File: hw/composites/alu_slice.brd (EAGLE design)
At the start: 50 x 50 mm, 10 parts, among them CON2 GENERIC-2X10

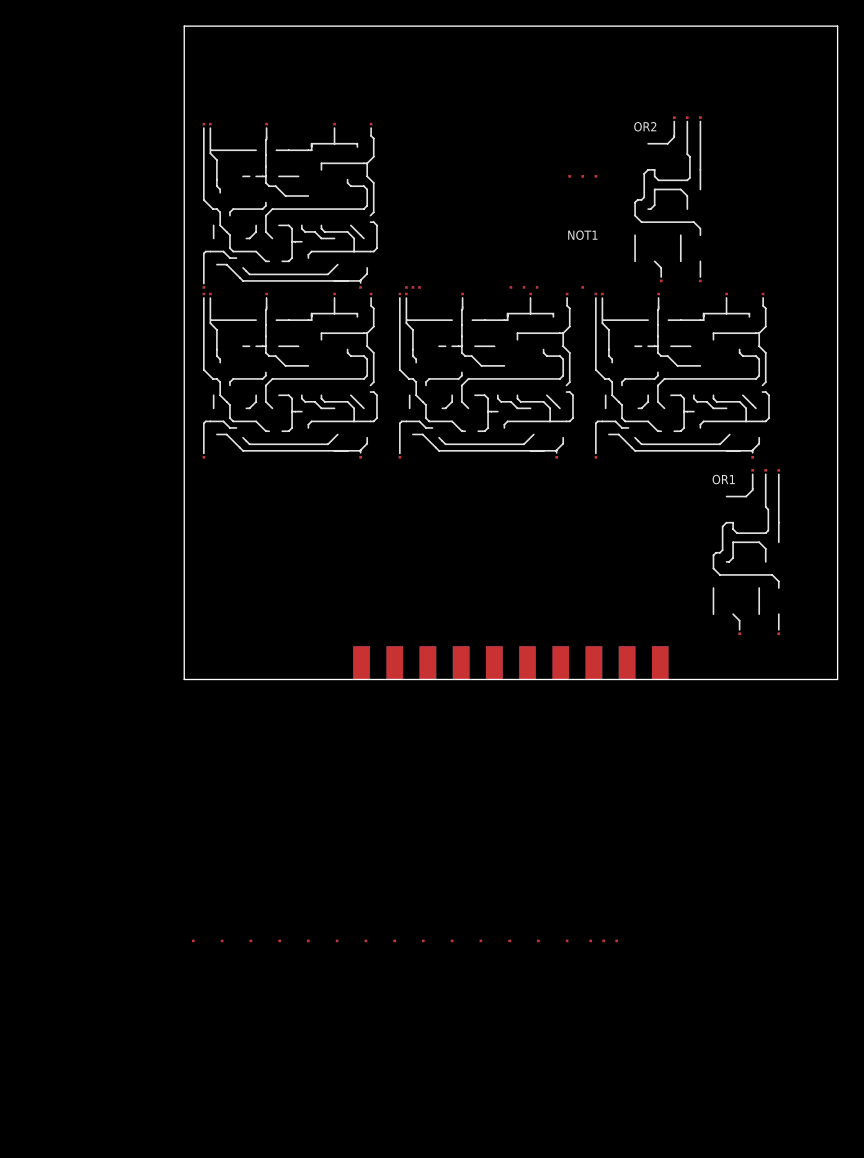
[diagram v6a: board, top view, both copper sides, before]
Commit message: Add led output and prepare first alu slice
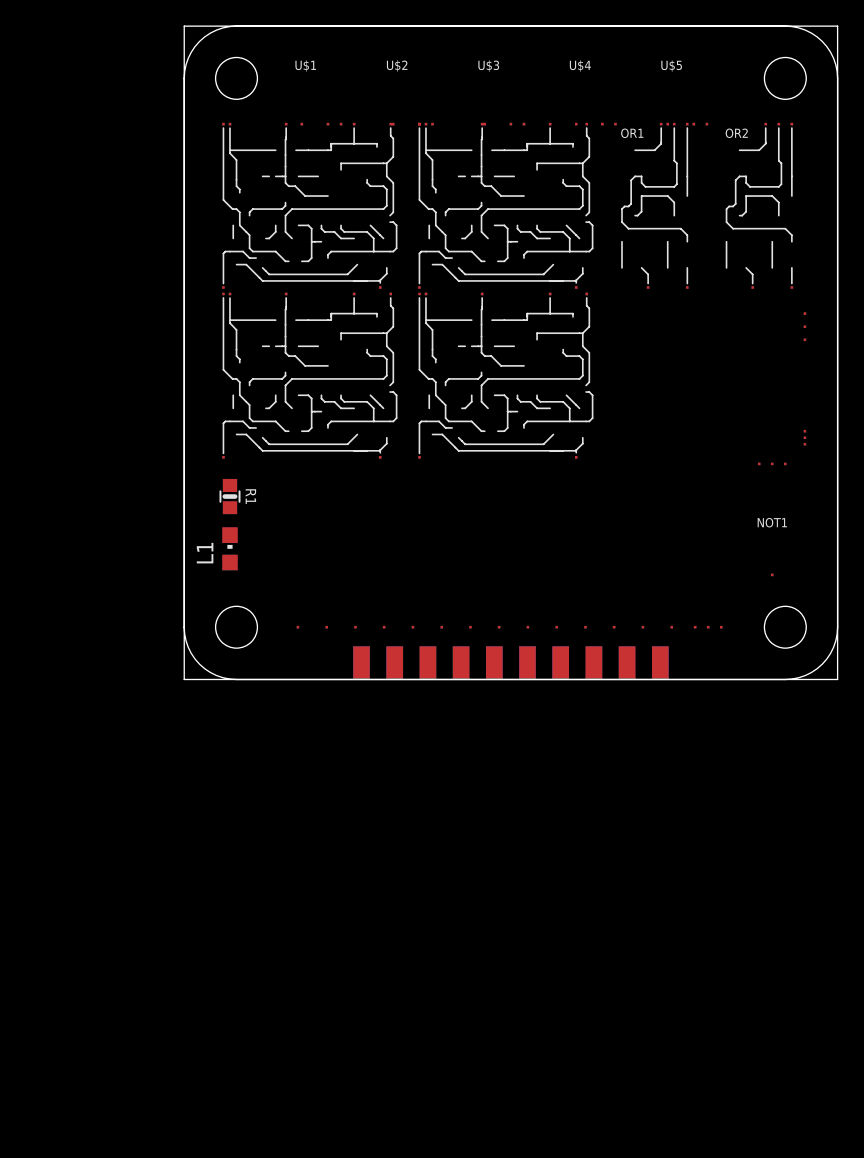
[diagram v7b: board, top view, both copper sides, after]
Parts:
- added L1: (no value), p.peter-leds:CHIPLED_0805
- added PCB1: PCB_DP_SQUARE-5X5, dp_pcb:DP5050_V1
- added R1: 1k, p.peter-rcl:R0603-MARK
- added U$1, U$2, U$3, U$4, U$5: LEDDRIVER, p.peter-gator:LEDDRIVER
- moved SEL1 34.1 mm to (47.5, 17.0), turned to 90 degrees
- moved OR1 27.4 mm to (32.5, 30.0)
- moved NOT1 26.3 mm to (43.0, 8.00)
- moved SEL3 25.3 mm to (7.50, 4.00)
- moved XOR4 18.7 mm to (17.5, 30.0)
- moved OR2 7.02 mm to (40.5, 30.0)
- moved XOR1 1.50 mm to (2.50, 17.0)
- moved XOR2 1.50 mm to (2.50, 30.0)
- moved XOR3 1.50 mm to (17.5, 17.0)
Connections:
- new net N$6: L1.C, R1.2
- net +5V: now also L1.A, U$1._VP, U$2._VP, U$3._VP, U$4._VP, U$5._VP
- net A: now also U$1.A
- net B: now also U$2.A
- net CARRY_IN: now also U$3.A
- net CARRY_OUT: now also U$5.A
- net GND: now also R1.1, U$1._VN, U$2._VN, U$3._VN, U$4._VN, U$5._VN
- net RESULT: now also U$4.A
